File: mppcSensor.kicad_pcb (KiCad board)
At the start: 2 copper layers, 5 x 5 mm, 2 parts, among them J1 Conn_Coaxial

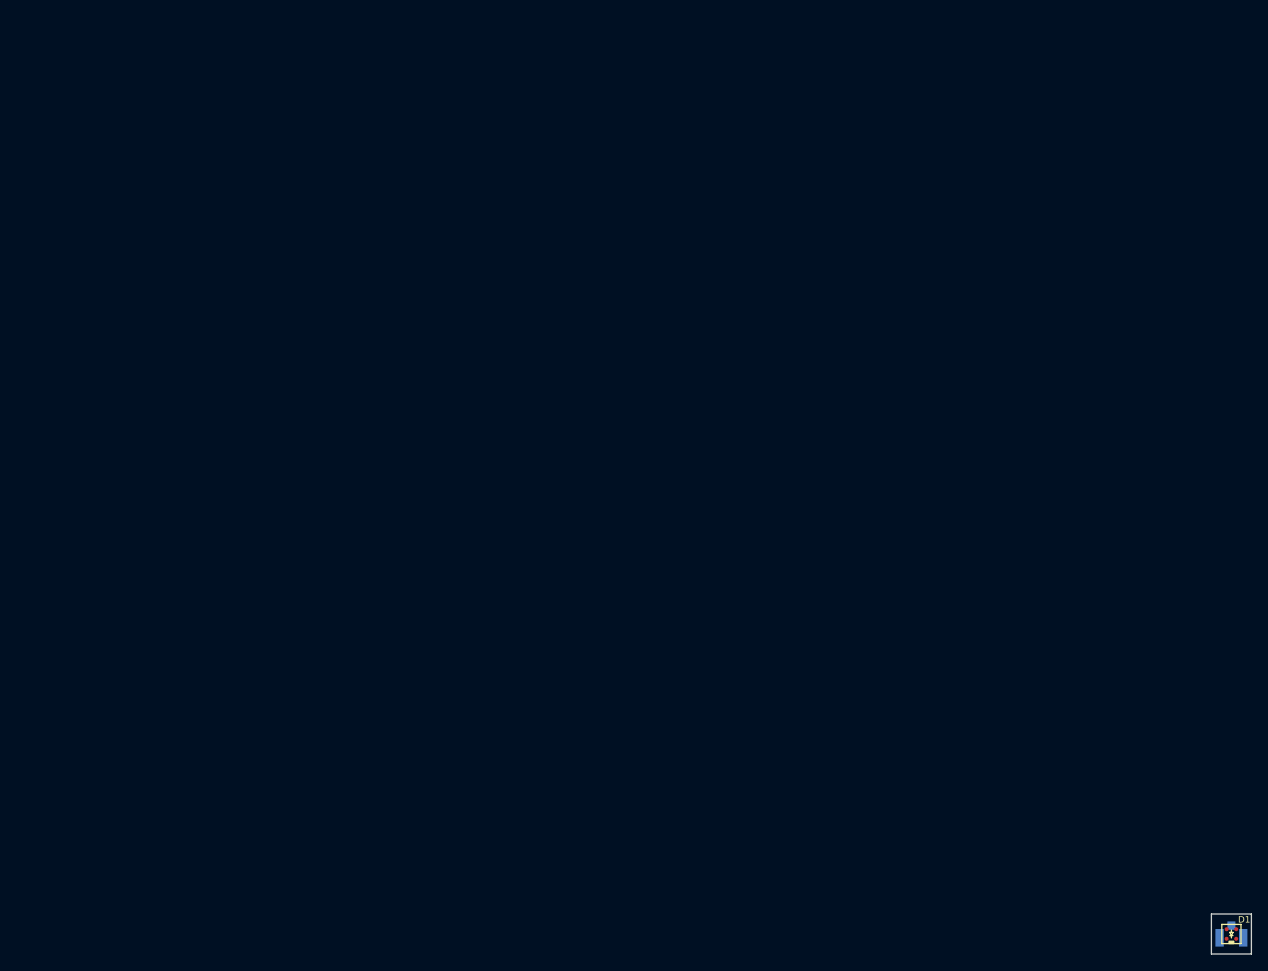
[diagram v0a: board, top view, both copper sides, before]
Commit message: Changed to kicad, sensor only boards
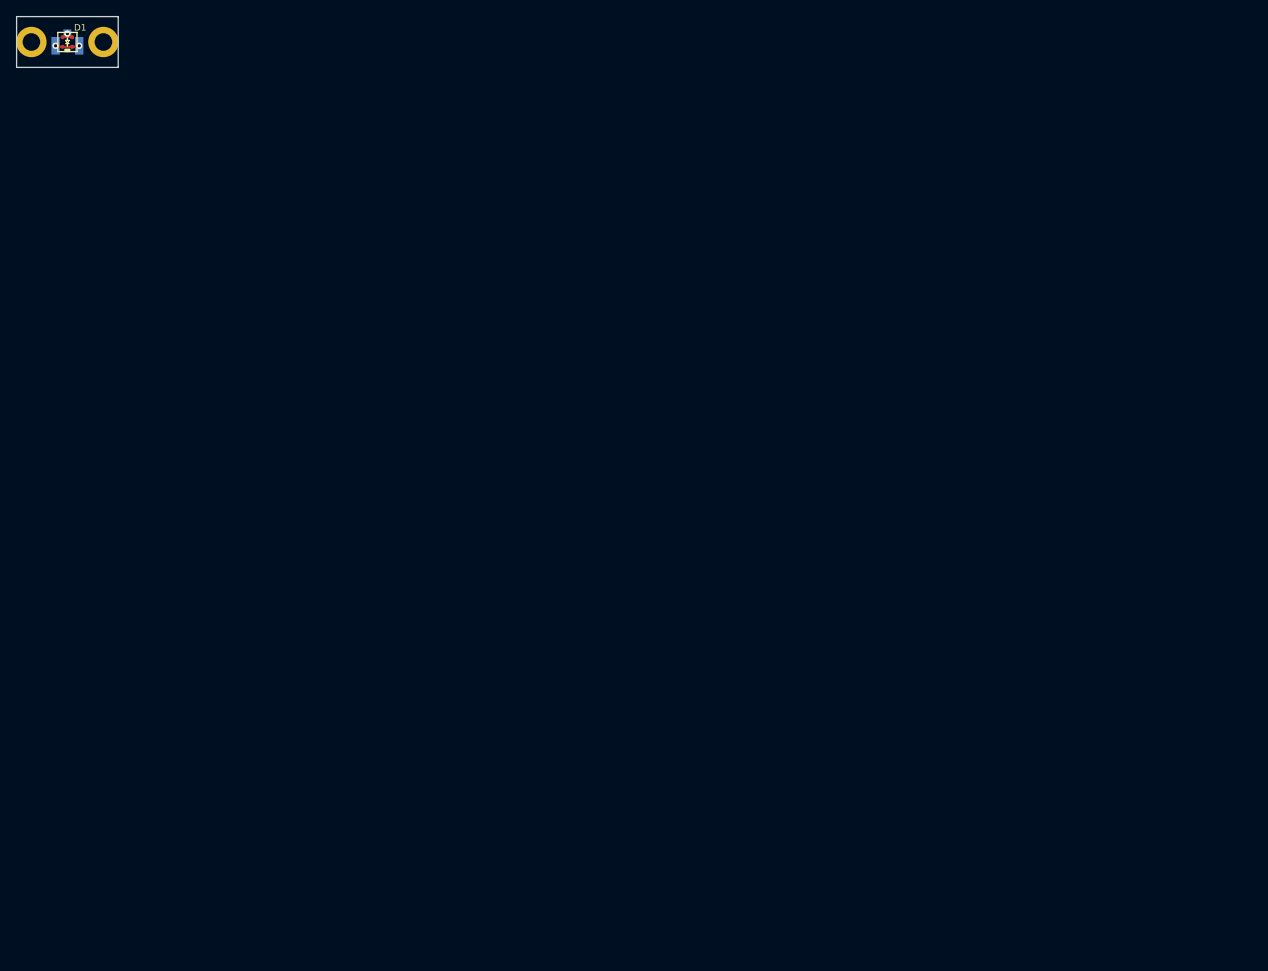
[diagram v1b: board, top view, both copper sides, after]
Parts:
- added H1: MountingHole, MountingHole:MountingHole_2.2mm_M2_ISO14580_Pad, F.Cu at (-4.50, 0.00)
- added H2: MountingHole, MountingHole:MountingHole_2.2mm_M2_ISO14580_Pad, F.Cu at (4.50, 0.00)
- moved D1 183.3 mm to (0.00, 0.00)
- moved J1 183.3 mm to (0.00, 0.00)
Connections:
- D1 pad 1: (no net) -> Net-(D1-Pad1)
- D1 pad 2: (no net) -> Net-(D1-Pad2)
- J1 pad 1: Net-(D1-PadA) -> Net-(D1-Pad1)
- J1 pad 2: Net-(D1-PadK) -> Net-(D1-Pad2)
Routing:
- net Net-(D1-Pad2): track 0.00 -> 3.05 mm, vias 0 -> 2
- net Net-(D1-Pad1): track 0.00 -> 1.65 mm, vias 0 -> 1
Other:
- board size 5 x 5 mm -> 12.7 x 6.3 mm
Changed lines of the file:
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@@
-(kicad_pcb (version 20171130) (host pcbnew "(5.0.2)-1")
+(kicad_pcb (version 20171130) (host pcbnew "(5.0.1)-4")
   (general
     (thickness 1.6)
-    (drawings 4)
-    (tracks 0)
+    (drawings 8)
+    (tracks 11)
     (zones 0)
-    (modules 2)
+    (modules 4)
     (nets 3)
   )
@@
     (zone_45_only no)
     (trace_min 0.2)
-    (segment_width 0.2)
+    (segment_width 0.15)
     (edge_width 0.15)
     (via_size 0.8)
@@
     (mod_text_size 1 1)
     (mod_text_width 0.15)
-    (pad_size 1.524 1.524)
-    (pad_drill 0.762)
+    (pad_size 3.8 3.8)
+    (pad_drill 2.2)
     (pad_to_mask_clearance 0.051)
     (solder_mask_min_width 0.25)
     (aux_axis_origin 0 0)
-    (visible_elements FFFFFF7F)
+    (visible_elements 7EFFFFFF)
     (pcbplotparams
       (layerselection 0x010fc_ffffffff)
@@
   )
   (net 0 "")
-  (net 1 "Net-(D1-PadK)")
-  (net 2 "Net-(D1-PadA)")
+  (net 1 "Net-(D1-Pad2)")
+  (net 2 "Net-(D1-Pad1)")
   (net_class Default "This is the default net class."
     (clearance 0.2)
@@
     (uvia_dia 0.3)
     (uvia_drill 0.1)
-    (add_net "Net-(D1-PadA)")
-    (add_net "Net-(D1-PadK)")
+    (add_net "Net-(D1-Pad1)")
+    (add_net "Net-(D1-Pad2)")
   )
   (module Connector_Coaxial:U.FL_Hirose_U.FL-R-SMT-1_Vertical (layer B.Cu)
-    (at 145.5 111.5 270)
+    (at 0 0 270)
     (descr "Hirose U.FL Coaxial https://www.hirose.com/product/en/products/U.FL/U.FL-R-SMT-1%2810%29/")
     (tags "Hirose U.FL Coaxial")
@@
     (fp_line (start -1.32 1) (end -2.02 1) (layer B.CrtYd) (width 0.05))
     (pad 2 smd rect (at 0.475 -1.475 270) (size 2.2 1.05) (layers B.Cu B.Paste B.Mask)
-      (net 1 "Net-(D1-PadK)"))
+      (net 1 "Net-(D1-Pad2)"))
     (pad 1 smd rect (at -1.05 0 270) (size 1.05 1) (layers B.Cu B.Paste B.Mask)
-      (net 2 "Net-(D1-PadA)"))
+      (net 2 "Net-(D1-Pad1)"))
     (pad 2 smd rect (at 0.475 1.475 270) (size 2.2 1.05) (layers B.Cu B.Paste B.Mask)
-      (net 1 "Net-(D1-PadK)"))
+      (net 1 "Net-(D1-Pad2)"))
     (model ${KISYS3DMOD}/Connector_Coaxial.3dshapes/U.FL_Hirose_U.FL-R-SMT-1_Vertical.wrl
       (offset (xyz 0.4749999928262157 0 0))
@@
   )
   (module s13360-2050ve:S13360-2050VE (layer F.Cu)
-    (at 145.5 111.5)
+    (at 0 0)
     (fp_text reference D1 (at 1.6 -1.8) (layer F.SilkS)
       (effects (font (size 0.8 0.8) (thickness 0.1)))
@@
       (effects (font (size 1 1) (thickness 0.15)))
     )
-    (pad 2 smd circle (at -0.6 0.6) (size 0.5 0.5) (layers F.Cu F.Paste F.Mask))
-    (pad 2 smd circle (at 0.6 0.6) (size 0.5 0.5) (layers F.Cu F.Paste F.Mask))
-    (pad 1 smd circle (at 0.6 -0.6) (size 0.5 0.5) (layers F.Cu F.Paste F.Mask))
-    (pad 1 smd circle (at -0.6 -0.6) (size 0.5 0.5) (layers F.Cu F.Paste F.Mask))
+    (pad 2 smd circle (at -0.6 0.6) (size 0.5 0.5) (layers F.Cu F.Paste F.Mask)
+      (net 1 "Net-(D1-Pad2)"))
+    (pad 2 smd circle (at 0.6 0.6) (size 0.5 0.5) (layers F.Cu F.Paste F.Mask)
+      (net 1 "Net-(D1-Pad2)"))
+    (pad 1 smd circle (at 0.6 -0.6) (size 0.5 0.5) (layers F.Cu F.Paste F.Mask)
+      (net 2 "Net-(D1-Pad1)"))
+    (pad 1 smd circle (at -0.6 -0.6) (size 0.5 0.5) (layers F.Cu F.Paste F.Mask)
+      (net 2 "Net-(D1-Pad1)"))
     (model ${KIPRJMOD}/components/s13360-2050ve/s13360-2050ve.stp
       (at (xyz 0 0 0))
@@
     )
   )
-  (gr_line (start 143 114) (end 148 114) (layer Edge.Cuts) (width 0.15))
-  (gr_line (start 143 109) (end 143 114) (layer Edge.Cuts) (width 0.15))
-  (gr_line (start 148 109) (end 143 109) (layer Edge.Cuts) (width 0.15))
-  (gr_line (start 148 114) (end 148 109) (layer Edge.Cuts) (width 0.15))
+  (module MountingHole:MountingHole_2.2mm_M2_ISO14580_Pad (layer F.Cu)
+    (at -4.5 0)
+    (descr "Mounting Hole 2.2mm, M2, ISO14580")
+    (tags "mounting hole 2.2mm m2 iso14580")
+    (attr virtual)
+    (fp_text reference H1 (at 0 -2.9) (layer F.SilkS) hide
+      (effects (font (size 1 1) (thickness 0.15)))
+    )
+    (fp_text value MountingHole (at 0 2.9) (layer F.Fab)
+      (effects (font (size 1 1) (thickness 0.15)))
+    )
+    (fp_text user %R (at 0.3 0) (layer F.Fab)
+      (effects (font (size 1 1) (thickness 0.15)))
+    )
+    (fp_circle (center 0 0) (end 1.9 0) (layer Cmts.User) (width 0.15))
+    (fp_circle (center 0 0) (end 2.15 0) (layer F.CrtYd) (width 0.05))
+    (pad 1 thru_hole circle (at 0 0) (size 3.8 3.8) (drill 2.2) (layers *.Cu *.Mask))
+  )
+  (module MountingHole:MountingHole_2.2mm_M2_ISO14580_Pad (layer F.Cu)
+    (at 4.5 0)
+    (descr "Mounting Hole 2.2mm, M2, ISO14580")
+    (tags "mounting hole 2.2mm m2 iso14580")
+    (attr virtual)
+    (fp_text reference H2 (at 0 -2.9) (layer F.SilkS) hide
+      (effects (font (size 1 1) (thickness 0.15)))
+    )
+    (fp_text value MountingHole (at 0 2.9) (layer F.Fab)
+      (effects (font (size 1 1) (thickness 0.15)))
+    )
+    (fp_circle (center 0 0) (end 2.15 0) (layer F.CrtYd) (width 0.05))
+    (fp_circle (center 0 0) (end 1.9 0) (layer Cmts.User) (width 0.15))
+    (fp_text user %R (at 0.3 0) (layer F.Fab)
+      (effects (font (size 1 1) (thickness 0.15)))
+    )
+    (pad 1 thru_hole circle (at 0 0) (size 3.8 3.8) (drill 2.2) (layers *.Cu *.Mask))
+  )
+  (gr_line (start 6.35 3.175) (end 6.35 -3.175) (layer Edge.Cuts) (width 0.15))
+  (gr_line (start -6.35 3.175) (end 6.35 3.175) (layer Edge.Cuts) (width 0.15))
+  (gr_line (start -6.35 -3.175) (end -6.35 3.175) (layer Edge.Cuts) (width 0.15))
+  (gr_line (start 6.35 -3.175) (end -6.35 -3.175) (layer Edge.Cuts) (width 0.15))
+  (gr_line (start -2.5 2.5) (end 2.5 2.5) (layer F.CrtYd) (width 0.15))
+  (gr_line (start -2.5 -2.5) (end -2.5 2.5) (layer F.CrtYd) (width 0.15))
+  (gr_line (start 2.5 -2.5) (end -2.5 -2.5) (layer F.CrtYd) (width 0.15))
+  (gr_line (start 2.5 2.5) (end 2.5 -2.5) (layer F.CrtYd) (width 0.15))
+  (segment (start 0.6 0.6) (end -0.6 0.6) (width 0.25) (layer F.Cu) (net 1))
+  (via (at -1.475 0.475) (size 0.8) (drill 0.4) (layers F.Cu B.Cu) (net 1))
+  (segment (start -0.6 0.6) (end -1.35 0.6) (width 0.25) (layer F.Cu) (net 1))
+  (segment (start -1.35 0.6) (end -1.475 0.475) (width 0.25) (layer F.Cu) (net 1))
+  (via (at 1.475 0.475) (size 0.8) (drill 0.4) (layers F.Cu B.Cu) (net 1))
+  (segment (start 0.6 0.6) (end 1.35 0.6) (width 0.25) (layer F.Cu) (net 1))
+  (segment (start 1.35 0.6) (end 1.475 0.475) (width 0.25) (layer F.Cu) (net 1))
+  (via (at 0 -1.05) (size 0.8) (drill 0.4) (layers F.Cu B.Cu) (net 2))
+  (segment (start 0 -0.6) (end 0 -1.05) (width 0.25) (layer F.Cu) (net 2))
+  (segment (start -0.6 -0.6) (end 0 -0.6) (width 0.25) (layer F.Cu) (net 2))
+  (segment (start 0 -0.6) (end 0.6 -0.6) (width 0.25) (layer F.Cu) (net 2))
 )
